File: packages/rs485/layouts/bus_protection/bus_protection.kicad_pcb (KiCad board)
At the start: 2 copper layers, 10 parts

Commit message: Update build script and regenerate outputs
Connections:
- FL1 pad 1: line-3 -> line-2
- FL1 pad 2: line-1 -> line
- FL1 pad 3: line -> line-1
- FL1 pad 4: line-2 -> line-3
- R1 pad 1: line-1 -> line
- R2 pad 1: line-3 -> line-2
- R4 pad 1: line -> line-1
- R5 pad 1: line-2 -> line-3
- U1 pad 1: line-3 -> line-2
- U1 pad 2: line-1 -> line
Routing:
- net line-3: track 9.91 -> 2.02 mm
- net line-2: track 2.02 -> 9.91 mm
- net line-1: track 9.91 -> 2.02 mm
- net line: track 2.02 -> 9.91 mm

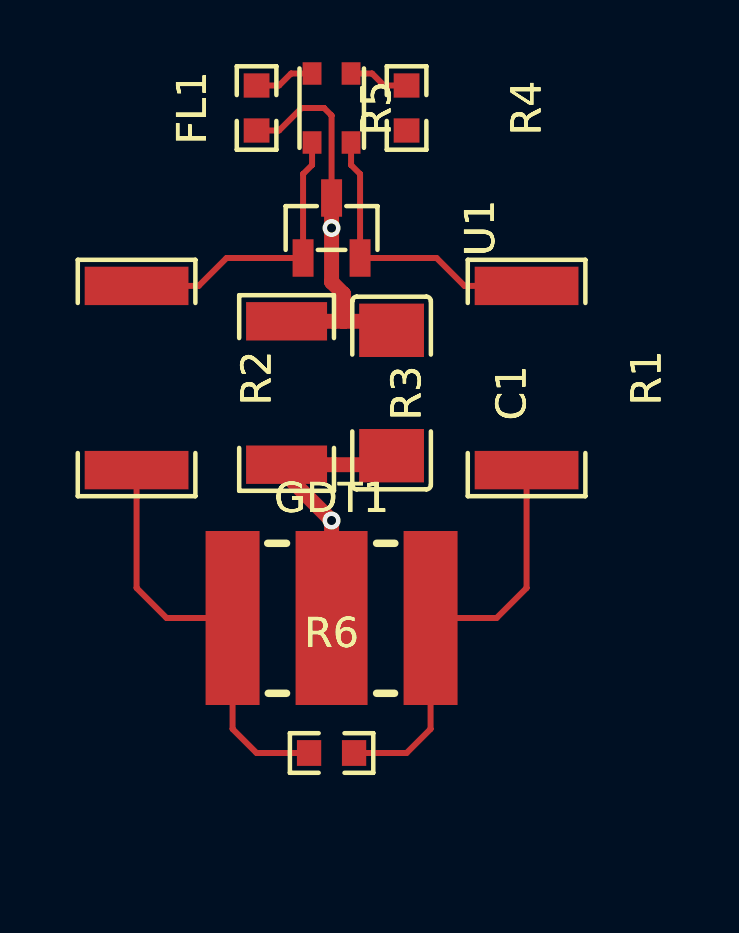
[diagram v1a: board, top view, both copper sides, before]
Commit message: Build all packages without designators on silkscreen.
Also disable fail_on_drc and enable keep_picked_parts for build
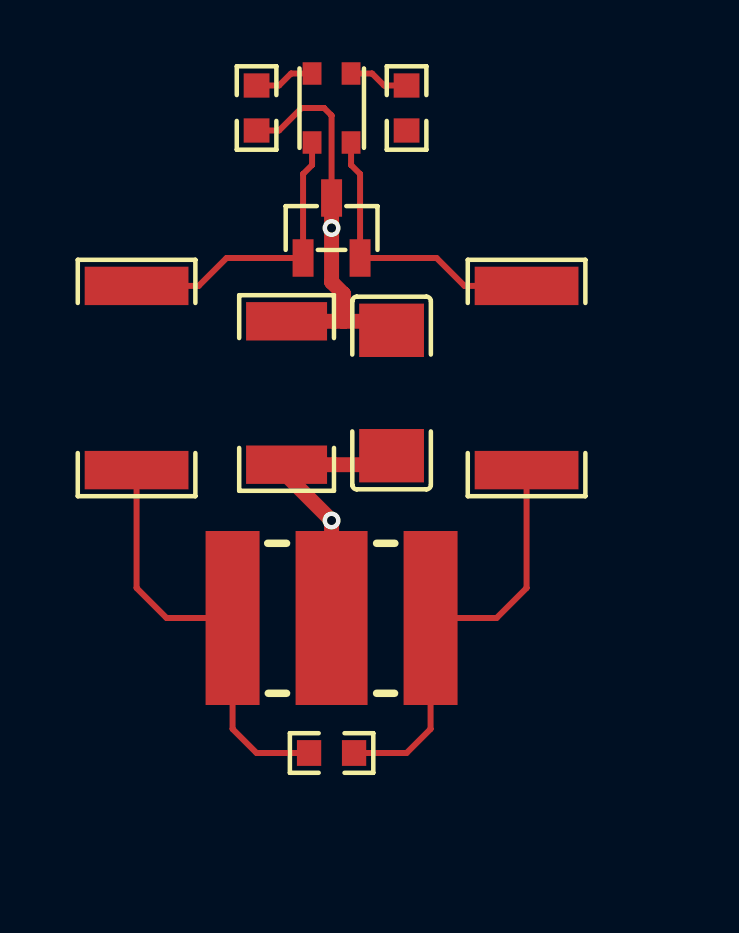
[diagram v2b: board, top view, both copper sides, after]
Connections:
- FL1 pad 2: line -> line-1
- FL1 pad 3: line-1 -> line
- R1 pad 1: line -> line-1
- R4 pad 1: line-1 -> line
- U1 pad 2: line -> line-1
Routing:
- net line-1: track 2.02 -> 9.91 mm
- net line: track 9.91 -> 2.02 mm
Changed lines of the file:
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@@
     (net 4 "earth")
     (net 5 "hv")
-    (net 6 "line")
-    (net 7 "line-1")
+    (net 6 "line-1")
+    (net 7 "line")
     (net 8 "gnd")
     (net 9 "line-2")
@@
             (at 0 -4.65 90)
             (layer "F.SilkS")
-            (hide no)
+            (hide yes)
             (effects
                 (font
@@
                     (thickness 0.15)
                 )
+                (hide yes)
             )
             (unlocked no)
@@
                     (thickness 0.15)
                 )
+                (hide yes)
             )
             (unlocked no)
@@
             (size 0.63 0.75)
             (layers "F.Cu" "F.Mask" "F.Paste")
-            (net 6 "line")
+            (net 6 "line-1")
         )
         (pad "3" smd rect
@@
             (size 0.63 0.75)
             (layers "F.Cu" "F.Mask" "F.Paste")
-            (net 7 "line-1")
+            (net 7 "line")
         )
         (pad "4" smd rect
@@
             (at 0 -4 0)
             (layer "F.SilkS")
-            (hide no)
+            (hide yes)
             (effects
                 (font
@@
                     (thickness 0.15)
                 )
+                (hide yes)
             )
             (unlocked no)
@@
                     (thickness 0.15)
                 )
+                (hide yes)
             )
             (unlocked no)
@@
             (at 0 -4 90)
             (layer "F.SilkS")
-            (hide no)
+            (hide yes)
             (effects
                 (font
@@
                     (thickness 0.15)
                 )
+                (hide yes)
             )
             (unlocked no)
@@
                     (thickness 0.15)
                 )
+                (hide yes)
             )
             (unlocked no)
@@
             (size 0.81 0.86)
             (layers "F.Cu" "F.Mask" "F.Paste")
-            (net 7 "line-1")
+            (net 7 "line")
         )
         (pad "2" smd rect
@@
             (at 0 -4 0)
             (layer "F.SilkS")
-            (hide no)
+            (hide yes)
             (effects
                 (font
@@
                     (thickness 0.15)
                 )
+                (hide yes)
             )
             (unlocked no)
@@
                     (thickness 0.15)
                 )
+                (hide yes)
             )
             (unlocked no)
@@
             (at 0 -4 90)
             (layer "F.SilkS")
-            (hide no)
+            (hide yes)
             (effects
                 (font
@@
                     (thickness 0.15)
                 )
+                (hide yes)
             )
             (unlocked no)
@@
                     (thickness 0.15)
                 )
+                (hide yes)
             )
             (unlocked no)
@@
             (size 1.28 3.46)
             (layers "F.Cu" "F.Mask" "F.Paste")
-            (net 6 "line")
+            (net 6 "line-1")
         )
         (pad "2" smd rect
@@
             (at 0 -4.95 90)
             (layer "F.SilkS")
-            (hide no)
+            (hide yes)
             (effects
                 (font
@@
                     (thickness 0.15)
                 )
+                (hide yes)
             )
             (unlocked no)
@@
                     (thickness 0.15)
                 )
+                (hide yes)
             )
             (unlocked no)
@@
             (size 1.25 0.7)
             (layers "F.Cu" "F.Mask" "F.Paste")
-            (net 6 "line")
+            (net 6 "line-1")
         )
         (pad "3" smd rect
@@
             (at 0 -4 90)
             (layer "F.SilkS")
-            (hide no)
+            (hide yes)
             (effects
                 (font
@@
                     (thickness 0.15)
                 )
+                (hide yes)
             )
             (unlocked no)
@@
                     (thickness 0.15)
                 )
+                (hide yes)
             )
             (unlocked no)
@@
             (at 0 -4 90)
             (layer "F.SilkS")
-            (hide no)
+            (hide yes)
             (effects
                 (font
@@
                     (thickness 0.15)
                 )
+                (hide yes)
             )
             (unlocked no)
@@
                     (thickness 0.15)
                 )
+                (hide yes)
             )
             (unlocked no)
@@
             (at 0 -4 90)
             (layer "F.SilkS")
-            (hide no)
+            (hide yes)
             (effects
                 (font
@@
                     (thickness 0.15)
                 )
+                (hide yes)
             )
             (unlocked no)
@@
                     (thickness 0.15)
                 )
+                (hide yes)
             )
             (unlocked no)
@@
             (at 0 -4 90)
             (layer "F.SilkS")
-            (hide no)
+            (hide yes)
             (effects
                 (font
@@
                     (thickness 0.15)
                 )
+                (hide yes)
             )
             (unlocked no)
@@
                     (thickness 0.15)
                 )
+                (hide yes)
             )
             (unlocked no)

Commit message: Rebuild rs485 package
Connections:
- FL1 pad 1: line-2 -> line
- FL1 pad 2: line-1 -> line-3
- FL1 pad 3: line -> line-2
- FL1 pad 4: line-3 -> line-1
- R1 pad 1: line-1 -> line-3
- R2 pad 1: line-2 -> line
- R4 pad 1: line -> line-2
- R5 pad 1: line-3 -> line-1
- U1 pad 1: line-2 -> line
- U1 pad 2: line-1 -> line-3
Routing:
- net line-3: track 2.02 -> 9.91 mm
- net line-2: track 9.91 -> 2.02 mm
- net line-1: track 9.91 -> 2.02 mm
- net line: track 2.02 -> 9.91 mm
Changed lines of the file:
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@@
     (net 0 "")
     (net 1 "tube_1")
-    (net 2 "line-3")
+    (net 2 "line-1")
     (net 3 "tube_2")
     (net 4 "earth")
     (net 5 "hv")
-    (net 6 "line-1")
-    (net 7 "line")
+    (net 6 "line-3")
+    (net 7 "line-2")
     (net 8 "gnd")
-    (net 9 "line-2")
+    (net 9 "line")
     (footprint "atopile:FILTER-SMD_4P-L2.5-W2.0-BL-83ef72"
         (layer "F.Cu")
@@
             (size 0.63 0.75)
             (layers "F.Cu" "F.Mask" "F.Paste")
-            (net 9 "line-2")
+            (net 9 "line")
         )
         (pad "2" smd rect
@@
             (size 0.63 0.75)
             (layers "F.Cu" "F.Mask" "F.Paste")
-            (net 6 "line-1")
+            (net 6 "line-3")
         )
         (pad "3" smd rect
@@
             (size 0.63 0.75)
             (layers "F.Cu" "F.Mask" "F.Paste")
-            (net 7 "line")
+            (net 7 "line-2")
         )
         (pad "4" smd rect
@@
             (size 0.63 0.75)
             (layers "F.Cu" "F.Mask" "F.Paste")
-            (net 2 "line-3")
+            (net 2 "line-1")
         )
         (embedded_fonts no)
@@
             (size 0.81 0.86)
             (layers "F.Cu" "F.Mask" "F.Paste")
-            (net 7 "line")
+            (net 7 "line-2")
         )
         (pad "2" smd rect
@@
             (size 1.28 3.46)
             (layers "F.Cu" "F.Mask" "F.Paste")
-            (net 6 "line-1")
+            (net 6 "line-3")
         )
         (pad "2" smd rect
@@
             (size 1.25 0.7)
             (layers "F.Cu" "F.Mask" "F.Paste")
-            (net 9 "line-2")
+            (net 9 "line")
         )
         (pad "2" smd rect
@@
             (size 1.25 0.7)
             (layers "F.Cu" "F.Mask" "F.Paste")
-            (net 6 "line-1")
+            (net 6 "line-3")
         )
         (pad "3" smd rect
@@
             (size 0.81 0.86)
             (layers "F.Cu" "F.Mask" "F.Paste")
-            (net 2 "line-3")
+            (net 2 "line-1")
         )
         (pad "2" smd rect
@@
             (size 1.28 3.46)
             (layers "F.Cu" "F.Mask" "F.Paste")
-            (net 9 "line-2")
+            (net 9 "line")
         )
         (pad "2" smd rect

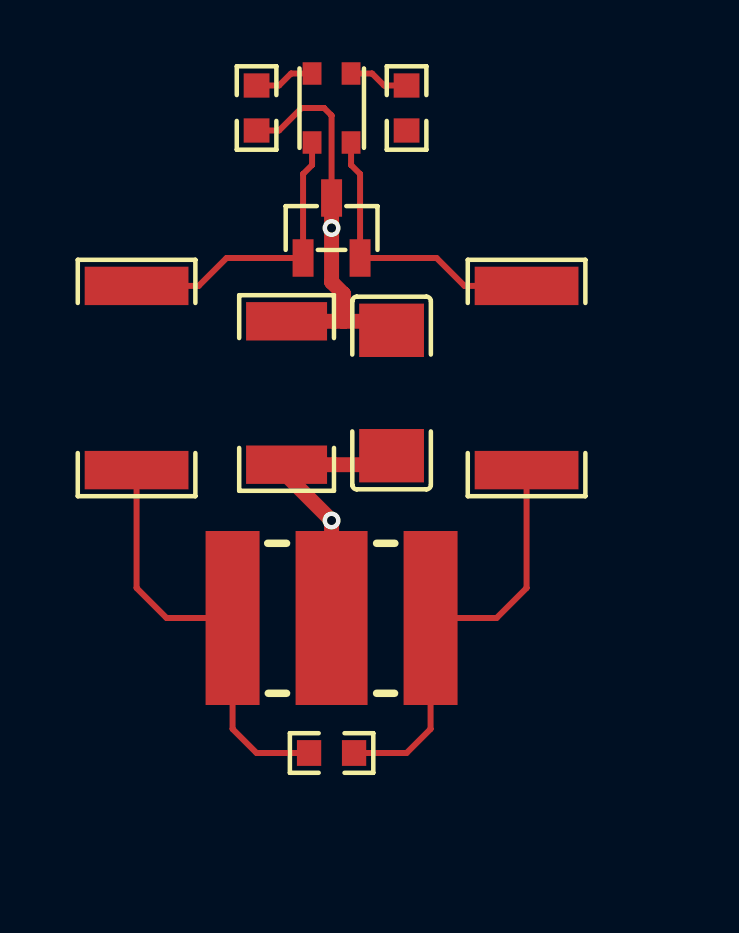
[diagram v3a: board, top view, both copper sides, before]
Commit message: Add various new packages (#14)
Add:
- DCDC converters
- Connectors

Update:
- logic
  - add dual buffer
- ldos
  - change to better default ldo
- usb
  - add missing connection
- switches
  - update rotary encoder advanced layout
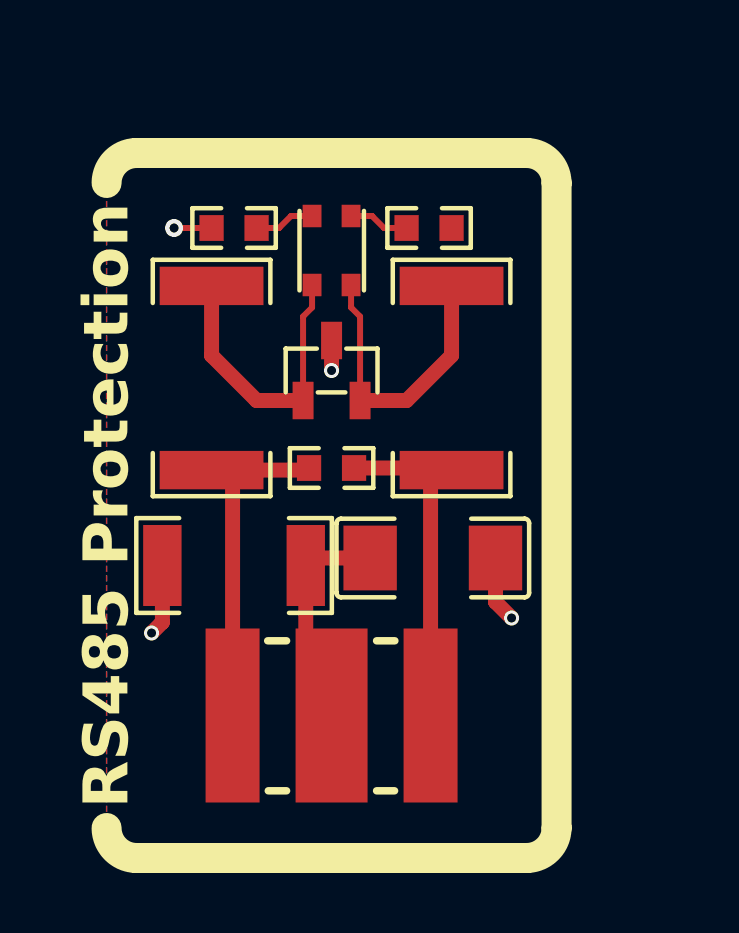
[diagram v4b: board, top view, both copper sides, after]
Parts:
- moved R6 9.50 mm to (0.00, -5.00)
- moved R3 6.01 mm to (-3.25, -1.75), turned to 0 degrees
- moved C1 5.67 mm to (3.38, -2.00), turned to 180 degrees
- moved FL1 4.75 mm to (0.00, -12.2)
- moved U1 4.75 mm to (0.00, -8.25)
- moved R4 4.07 mm to (3.25, -13.0), turned to 0 degrees
- moved R5 4.07 mm to (-3.25, -13.0), turned to 180 degrees
- moved GDT1 3.25 mm to (0.00, 3.25)
- moved R1 2.50 mm to (4.00, -8.00)
- moved R2 2.50 mm to (-4.00, -8.00)
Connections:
- FL1 pad 1: line -> line-2
- FL1 pad 2: line-3 -> line
- FL1 pad 3: line-2 -> line-3
- R1 pad 1: line-3 -> line
- R2 pad 1: line -> line-2
- R4 pad 1: line-2 -> line-3
- U1 pad 1: line -> line-2
- U1 pad 2: line-3 -> line
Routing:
- net line-2: track 2.02 -> 9.97 mm
- net line-3: track 9.91 -> 2.02 mm
- net gnd: track 13.6 -> 6.87 mm, vias 1 -> 4
- net tube_2: track 14.1 -> 12.2 mm
- net tube_1: track 14.1 -> 12.2 mm
- net earth: track 9.36 -> 8.25 mm, vias 1 -> 0
- added copper zone on B.Cu, net gnd
- added copper zone on F.Cu, net gnd
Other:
- board text added: "RS485 Protection"

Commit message: Rebuild all
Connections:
- FL1 pad 1: line-2 -> line-1
- FL1 pad 2: line -> line-3
- FL1 pad 3: line-3 -> line
- FL1 pad 4: line-1 -> line-2
- R1 pad 1: line -> line-3
- R2 pad 1: line-2 -> line-1
- R4 pad 1: line-3 -> line
- R5 pad 1: line-1 -> line-2
- U1 pad 1: line-2 -> line-1
- U1 pad 2: line -> line-3
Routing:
- net line-3: track 2.02 -> 9.97 mm
- net line-2: track 9.97 -> 2.02 mm
- net line-1: track 2.02 -> 9.97 mm
- net line: track 9.97 -> 2.02 mm

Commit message: WIP update rs485
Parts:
- C1: footprint atopile:C1808-cc38be -> IHHEC_C1808X102K202T:C1808
- FL1: footprint atopile:FILTER-SMD_4P-L2.5-W2.0-BL-83ef72 -> TDK_ACM2520_301_2P_T002:FILTER-SMD_4P-L2.5-W2.0-BL
- GDT1: footprint atopile:DIO-DT-SMD_L7.2-W5.0-9a878e -> Brightking_Elec_3RL090M_5_S:DIO-DT-SMD_L7.2-W5.0
- R1, R2: value 2.7Ω ±1% 1W -> 2.7Ω ±5% 1W; footprint atopile:R2512-78e9bd -> FOJAN_FRC2512J2R7_TS:R2512
- R3: footprint atopile:R2010-e92f2a -> Vishay_Intertech_RCV20101M00FKEFAT:R2010
- R4, R5: value 390Ω ±1% 100mW -> 390Ω ±1% 125mW; footprint atopile:R0603-ebcab9 -> UNI_ROYAL_0805W8F3900T5E:R0805
- R6: footprint atopile:R0603-ebcab9 -> UNI_ROYAL_0603WAF1200T5E:R0603
- U1: footprint atopile:SOT-23-3_L2.9-W1.3-P1.90-LS2.4-BR-688f29 -> ElecSuper_PSM712_ES:SOT-23-3_L2.9-W1.3-P1.90-LS2.4-BR
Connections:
- FL1 pad 2: line-3 -> line-2
- FL1 pad 3: line -> line-3
- FL1 pad 4: line-2 -> line
- R1 pad 1: line-3 -> line-2
- R4 pad 1: line -> line-3
- R5 pad 1: line-2 -> line
- U1 pad 2: line-3 -> line-2
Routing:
- net line-3: track 9.97 -> 2.02 mm
- net line-2: track 2.02 -> 9.97 mm

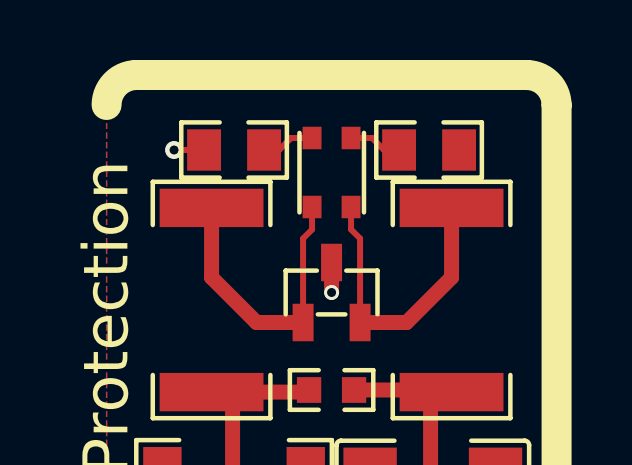
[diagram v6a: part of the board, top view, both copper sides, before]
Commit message: Manually fix fp lib tables
fix some small bugs
fix package only modules (e.g. logos)
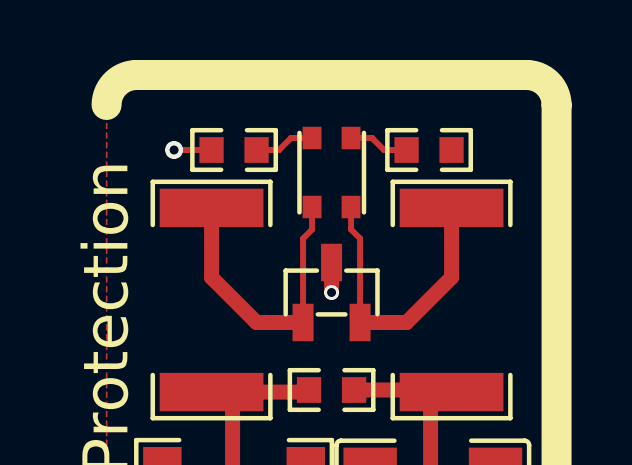
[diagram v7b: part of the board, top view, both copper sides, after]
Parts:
- R4, R5: value 390Ω ±1% 125mW -> 390Ω ±1% 100mW; footprint UNI_ROYAL_0805W8F3900T5E:R0805 -> UNI_ROYAL_0603WAF3900T5E:R0603
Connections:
- FL1 pad 1: line-1 -> line-2
- FL1 pad 2: line-2 -> line-1
- FL1 pad 3: line-3 -> line
- FL1 pad 4: line -> line-3
- R1 pad 1: line-2 -> line-1
- R2 pad 1: line-1 -> line-2
- R4 pad 1: line-3 -> line
- R5 pad 1: line -> line-3
- U1 pad 1: line-1 -> line-2
- U1 pad 2: line-2 -> line-1

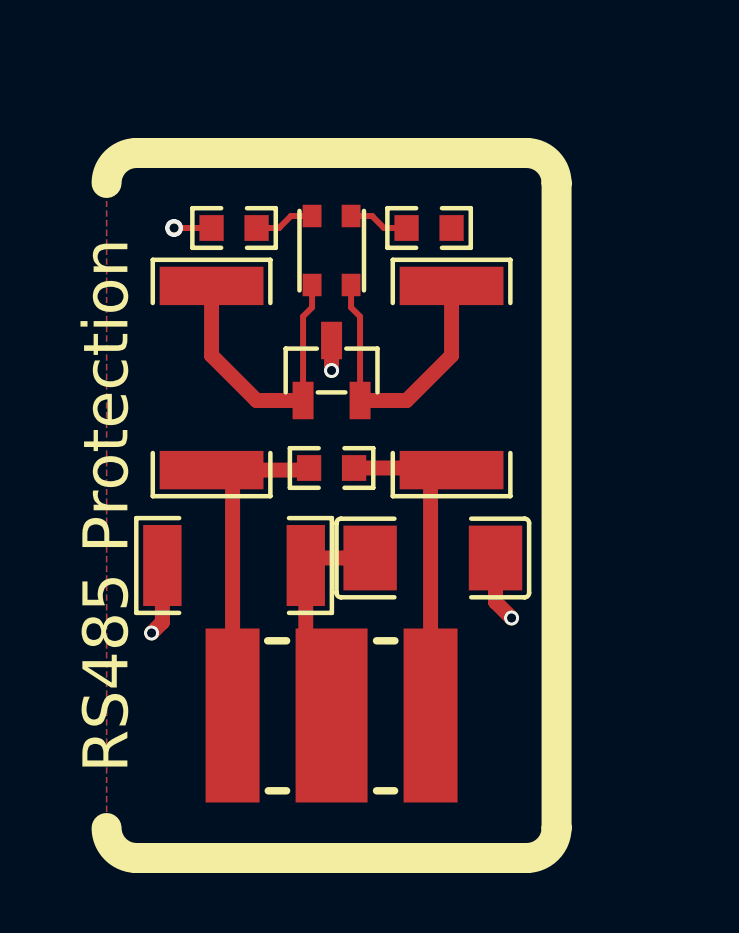
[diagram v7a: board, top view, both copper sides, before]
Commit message: Update 3D model locations
fix missing renders
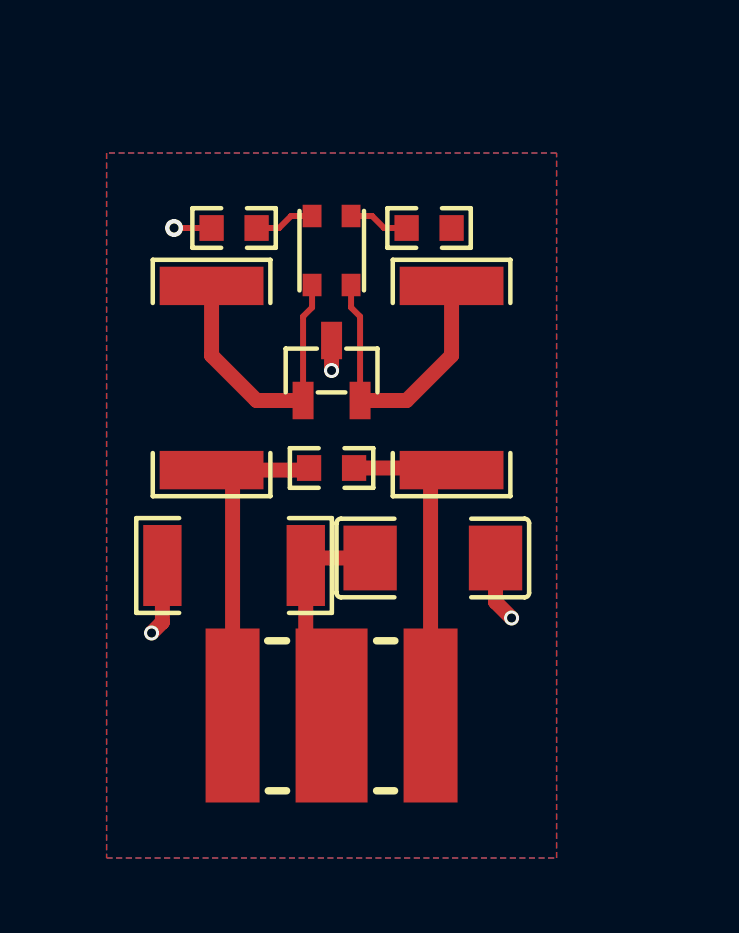
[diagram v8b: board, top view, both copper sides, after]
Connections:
- FL1 pad 1: line-2 -> line-3
- FL1 pad 3: line -> line-2
- FL1 pad 4: line-3 -> line
- R2 pad 1: line-2 -> line-3
- R4 pad 1: line -> line-2
- R5 pad 1: line-3 -> line
- U1 pad 1: line-2 -> line-3
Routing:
- net line-3: track 2.02 -> 9.97 mm
- net line-2: track 9.97 -> 2.02 mm
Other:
- board text removed: "RS485 Protection"
